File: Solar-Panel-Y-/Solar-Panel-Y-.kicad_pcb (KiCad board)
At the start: 6 copper layers, 64 x 58 mm, 67 parts, among them J1 FFC2B28-10-G, J2 BATTERY CONNECTOR, J3 B2B-PH-SM4-TB_LF__SN_, U1 Value, U2 TSL2561, U3 SW_SPDT, U4 SW_SPDT

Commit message: Exported Gerbers
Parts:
- added H1: MountingHole, MountingHole:MountingHole_2.2mm_M2_DIN965, F.Cu at (84.9, 44.5)
- added H2: MountingHole, MountingHole:MountingHole_2.2mm_M2_DIN965, F.Cu at (85.0, 84.3)
- added H3: MountingHole, MountingHole:MountingHole_2.2mm_M2_DIN965, F.Cu at (124.8, 84.3)
- added H4: MountingHole, MountingHole:MountingHole_2.2mm_M2_DIN965, F.Cu at (124.8, 44.5)
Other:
- outline, holes or cut-outs redrawn

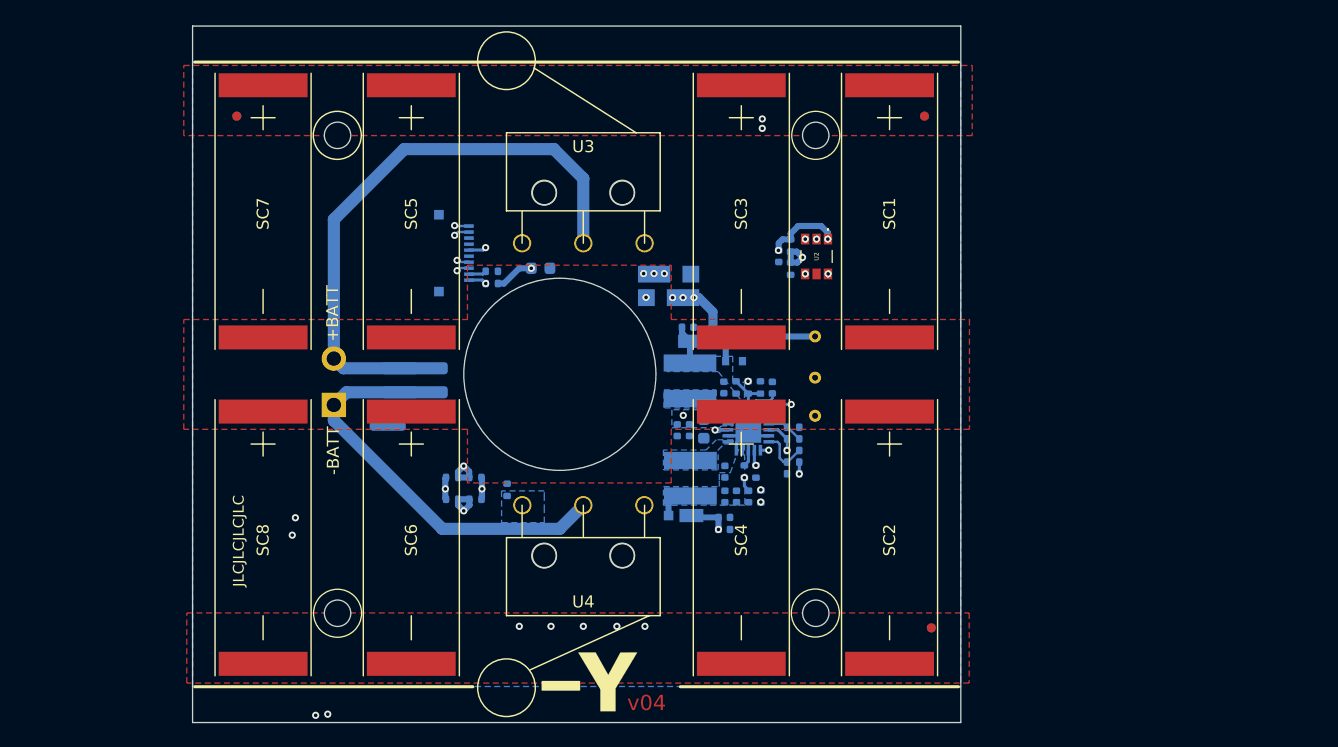
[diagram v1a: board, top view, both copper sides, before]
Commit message: X Board Changes for new Y rails
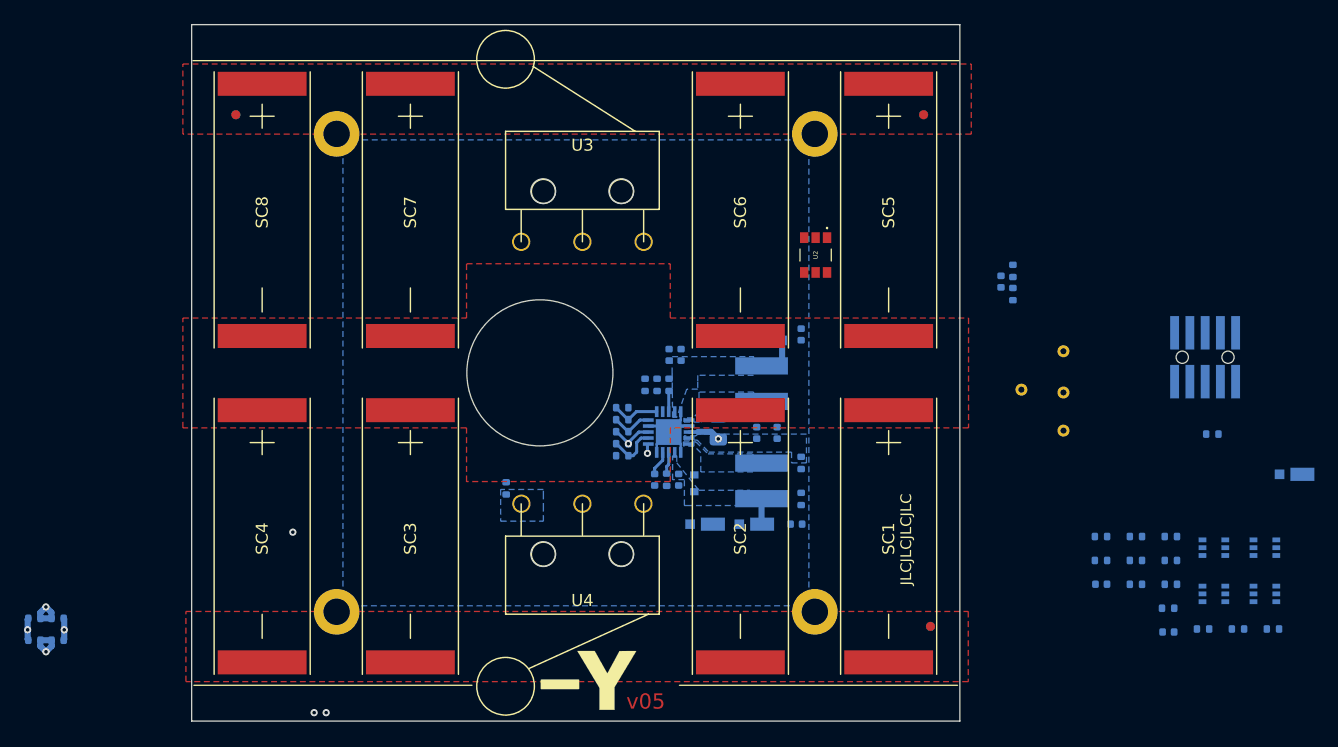
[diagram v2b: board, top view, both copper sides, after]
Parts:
- removed the C1 at (119.2, 74.6)
- removed C14: 100uF, Capacitor_SMD:C_0402_1005Metric
- removed the D5 at (112.5, 58.0)
- removed J2: BATTERY CONNECTOR, solarpanels:SCREWTERMINAL-3.5MM-2_LOCK
- removed J3: B2B-PH-SM4-TB_LF__SN_, Connector_JST:JST_PH_B2B-PH-SM4-TB_1x02-1MP_P2.00mm_Vertical
- removed the R1 at (118.8, 72.5)
- removed the R12 at (120.2, 65.5)
- removed the R13 at (119.2, 65.5)
- removed the R14 at (97.8, 56.9)
- removed the R7 at (119.8, 72.5)
- removed the R8 at (120.2, 74.6)
- added C5: 100uF, Capacitor_SMD:C_0805_2012Metric, B.Cu at (116.7, 68.9)
- added D3: MSS1P4-M3_89A, solarpanels:MICROSMP, B.Cu at (164.7, 72.8)
- added Q1: BSS138DWQ-7, Package_TO_SOT_SMD:SOT-363_SC-70-6, B.Cu at (162.2, 78.9)
- added Q2: MBT2222ADW1T1, Package_TO_SOT_SMD:SOT-363_SC-70-6, B.Cu at (157.9, 82.7)
- added Q3: BSS138DWQ-7, Package_TO_SOT_SMD:SOT-363_SC-70-6, B.Cu at (162.2, 82.7)
- added Q4: MBT2222ADW1T1, Package_TO_SOT_SMD:SOT-363_SC-70-6, B.Cu at (157.9, 78.9)
- added R10: 8.25M, Resistor_SMD:R_0402_1005Metric, B.Cu at (110.6, 65.3)
- added R11: 4.75M, Resistor_SMD:R_0402_1005Metric, B.Cu at (111.6, 65.3)
- added R16: 0, Resistor_SMD:R_0402_1005Metric, B.Cu at (123.6, 71.8)
- added R19: 0, Resistor_SMD:R_0402_1005Metric, B.Cu at (112.6, 65.3)
- added R21: 100K, Resistor_SMD:R_0402_1005Metric, B.Cu at (154.3, 79.9)
- added R22: 0, Resistor_SMD:R_0402_1005Metric, B.Cu at (154.3, 81.9)
- added R23: 0, Resistor_SMD:R_0402_1005Metric, B.Cu at (151.4, 77.9)
- added R24: 10K, Resistor_SMD:R_0402_1005Metric, B.Cu at (162.8, 85.6)
- added R25: 10K, Resistor_SMD:R_0402_1005Metric, B.Cu at (154.1, 83.9)
- added R26: 200K, Resistor_SMD:R_0402_1005Metric, B.Cu at (148.5, 77.9)
- added R27: 680, Resistor_SMD:R_0402_1005Metric, B.Cu at (159.9, 85.6)
- added R28: 100K, Resistor_SMD:R_0402_1005Metric, B.Cu at (151.4, 81.9)
- added R29: 10K, Resistor_SMD:R_0402_1005Metric, B.Cu at (154.3, 77.9)
- added R3: 0, Resistor_SMD:R_0402_1005Metric, B.Cu at (157.8, 69.4)
- added R30: 10K, Resistor_SMD:R_0402_1005Metric, B.Cu at (157.0, 85.6)
- added R31: 200K, Resistor_SMD:R_0402_1005Metric, B.Cu at (148.5, 79.9)
- added R4: 680, Resistor_SMD:R_0402_1005Metric, B.Cu at (151.4, 79.9)
- added TP4: TP, TestPoint:TestPoint_THTPad_D1.0mm_Drill0.5mm, B.Cu at (141.9, 65.7)
- C1: renamed from C5; value 0.1uF -> 1uF
- C10: value 100uF -> 0.1uF; footprint Capacitor_SMD:C_0603_1608Metric -> Capacitor_SMD:C_0402_1005Metric
- C12: value 100uF -> 10nF
- C13: value 0.1uF -> 10nF
- C6: value 100uF -> 1uF; footprint Capacitor_SMD:C_0603_1608Metric -> Capacitor_SMD:C_0402_1005Metric
- C7: value 22uF -> 4.7uF
- C8: value 4.7uF -> 22uF
- D1: value SDM20U40-7 -> SZMM5Z5V1T1G
- D4: value SBDiode -> MSS1P4-M3_89A; footprint solarpanels:SB Diode -> solarpanels:MICROSMP
- H1, H2, H3, H4: footprint MountingHole:MountingHole_2.2mm_M2_DIN965 -> MountingHole:MountingHole_2.2mm_M2_DIN965_Pad
- J1: value FFC2B28-10-G -> FTS-105-01-L-DV-A; footprint solarpanels:GCT_FFC2B28-10-G -> batteryboard:FTS-105-XX-YY-DV-A
- U1: value Value -> BQ25570RGRR
- moved J1 63.2 mm to (157.2, 63.0), turned to 180 degrees
- moved C13 38.0 mm to (154.1, 85.9), turned to 180 degrees
- moved R18 36.7 mm to (61.6, 84.7)
- moved R13 36.7 mm to (61.6, 86.6)
- moved R17 36.7 mm to (59.7, 84.7)
- moved R12 36.7 mm to (59.7, 86.6)
- moved C12 32.2 mm to (148.5, 81.9), turned to 180 degrees
- moved R15 32.0 mm to (123.6, 74.8), turned to 90 degrees
- moved D4 21.0 mm to (115.6, 76.9), turned to 180 degrees
- moved TP1 20.7 mm to (145.4, 69.1)
- moved TP2 20.7 mm to (145.4, 65.9)
- moved TP3 20.7 mm to (145.4, 62.5)
- moved C2 18.7 mm to (123.2, 76.9)
- moved C1 18.6 mm to (140.2, 56.7)
- moved R1 18.6 mm to (141.2, 55.8)
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- renumbered D3 to D5, R17 to R1, R9 to R12, R10 to R13, R11 to R14, R16 to R17, R19 to R18, R18 to R2, R2 to R5, R3 to R6, R4 to R7, R5 to R8, R6 to R9, SC2 to SC1, SC4 to SC2, SC6 to SC3, SC8 to SC4, SC1 to SC5, SC3 to SC6, SC5 to SC7, SC7 to SC8
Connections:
- C11 pad 1: Net-(C11-Pad1) -> +3V3
- C12 pad 1: Net-(C11-Pad1) -> Net-(C12-Pad1)
- C13 pad 1: +3V3 -> Net-(C13-Pad1)
- C6 pad 1: /VBAT -> VOUT_EN
- C7 pad 1: Net-(C11-Pad1) -> Net-(C7-Pad1)
- C9 pad 1: Net-(C10-Pad1) -> Net-(C7-Pad1)
- D2 pad 2: Net-(C11-Pad1) -> Net-(C10-Pad1)
- D4 pad 1: Net-(D4-Pad1) -> /VSOLAR_FULL
- D4 pad 2: GND -> Net-(D3-Pad1)
- J1 pad 1: BATT_P -> BATT_N_SW
- J1 pad 10: COIL_P -> VUSB
- J1 pad 2: BATT_N -> BATT_P_SW
- J1 pad 3: SDA1 -> BATT_P
- J1 pad 4: SCL1 -> +3V3
- J1 pad 5: BURN1 -> GND
- J1 pad 6: +3V3 -> SCL3
- J1 pad 7: GND -> COIL_P
- J1 pad 8: GND -> SDA3
- L2 pad 2: Net-(C11-Pad1) -> Net-(C10-Pad1)
- R14 pad 1: Net-(R11-Pad1) -> Net-(R14-Pad1)
- R15 pad 1: BATT_N -> GND
- R15 pad 2: GND -> Net-(R14-Pad1)
- SC1 pad 1: Net-(D4-Pad1) -> Net-(D3-Pad1)
- SC2 pad 1: Net-(D4-Pad1) -> Net-(D3-Pad1)
- SC3 pad 1: Net-(D4-Pad1) -> Net-(D3-Pad1)
- SC4 pad 1: Net-(D4-Pad1) -> Net-(D3-Pad1)
- SC5 pad 2: Net-(D4-Pad1) -> Net-(D3-Pad1)
- SC6 pad 2: Net-(D4-Pad1) -> Net-(D3-Pad1)
- SC7 pad 2: Net-(D4-Pad1) -> Net-(D3-Pad1)
- SC8 pad 2: Net-(D4-Pad1) -> Net-(D3-Pad1)
- TP1 pad 1: +3V3 -> VSOLAR
- TP3 pad 1: VSOLAR -> +3V3
- U1 pad 14: Net-(C11-Pad1) -> Net-(C10-Pad1)
- U1 pad 19: Net-(C10-Pad1) -> Net-(C7-Pad1)
- U1 pad 3: Net-(R11-Pad1) -> Net-(R14-Pad1)
- U2 pad 4: SCL1 -> SCL3
- U2 pad 6: SDA1 -> SDA3
- U3 pad 2: Net-(J2-Pad2) -> BATT_P_SW
- U4 pad 2: Net-(J2-Pad1) -> BATT_N_SW
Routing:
- net /coil: track 16701.1 -> 14508.4 mm, vias 6 -> 5
- net +3V3: track 68.9 -> 0.00 mm, vias 4 -> 0
- net Net-(J2-Pad2): track 48.3 -> 0.00 mm
- net Net-(J2-Pad1): track 33.8 -> 0.00 mm
- net SDA1: track 33.7 -> 0.00 mm, vias 2 -> 0
- net SCL1: track 31.2 -> 0.00 mm, vias 2 -> 0
- net /VBAT: track 32.2 -> 2.68 mm, vias 2 -> 1
- net COIL_P: track 31.3 -> 3.29 mm, vias 2 -> 1
- net /VSOLAR_FULL: track 25.0 -> 0.00 mm, vias 5 -> 0
- net COIL_N: track 26.6 -> 3.25 mm, vias 2 -> 1
- net VOUT_EN: track 12.2 -> 0.80 mm, vias 2 -> 1
- net VSOLAR: track 12.2 -> 2.04 mm
- net BATT_P: track 6.13 -> 0.00 mm, vias 1 -> 0
- net Net-(C10-Pad1): track 7.45 -> 1.52 mm, vias 2 -> 0
- net Net-(R1-Pad1): track 5.69 -> 0.00 mm, vias 2 -> 0
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- added copper zone on In3.Cu, net GND
- added copper zone on F.Cu, net Net-(D3-Pad1)
- removed copper zone on B.Cu, net Net-(C11-Pad1)
- removed copper zone on F.Cu, net Net-(D4-Pad1)
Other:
- outline, holes or cut-outs redrawn
- board text added: "v05"
- board text removed: "+BATT"
- board text removed: "-BATT"
- board text removed: "1"
- board text removed: "v04"

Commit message: Finished Y- Board
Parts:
- SW1: renamed from U3; footprint solarpanels:D2F-L2-2 -> solarpanels:D2F-L2-A1
- SW2: renamed from U4; footprint solarpanels:D2F-L2 -> solarpanels:D2F-L2-A
- moved D3 76.3 mm to (89.3, 60.5), turned to 0 degrees
- moved R12 59.4 mm to (118.7, 79.2), turned to 0 degrees
- moved R17 59.1 mm to (118.7, 81.1), turned to 0 degrees
- moved R13 55.6 mm to (116.8, 79.2), turned to 0 degrees
- moved R18 55.2 mm to (116.8, 81.1), turned to 0 degrees
- moved R24 47.8 mm to (119.3, 66.1), turned to 90 degrees
- moved Q1 46.1 mm to (118.9, 63.1), turned to -90 degrees
- moved Q3 44.7 mm to (118.9, 71.7), turned to -90 degrees
- moved J1 44.6 mm to (113.0, 68.7)
- moved R3 44.3 mm to (113.8, 74.1)
- moved R27 42.1 mm to (121.2, 69.1)
- moved C10 41.8 mm to (85.9, 79.3)
- moved Q2 41.1 mm to (121.8, 63.1), turned to -90 degrees
- moved C2 38.9 mm to (86.3, 64.3), turned to 180 degrees
- moved R21 38.7 mm to (118.2, 66.1), turned to 90 degrees
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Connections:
- C5 pad 1: /VBAT -> VBAT
- R3 pad 2: /VBAT -> VBAT
- TP4 pad 1: BATT_P -> VBAT
- U1 pad 18: /VBAT -> VBAT
- U2 pad 4: SCL3 -> SCL_LS
- U2 pad 6: SDA3 -> SDA_LS
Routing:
- net /coil: track 14508.4 -> 15508.4 mm
- net VBAT: track 0.00 -> 43.9 mm, vias 0 -> 2
- net BATT_P: track 0.00 -> 31.8 mm, vias 0 -> 1
- net +3V3: track 0.00 -> 25.1 mm, vias 0 -> 7
- net VSOLAR: track 2.04 -> 27.0 mm, vias 0 -> 1
- net /VSOLAR_FULL: track 0.00 -> 23.9 mm, vias 0 -> 4
- net SDA_LS: track 0.00 -> 23.5 mm, vias 0 -> 2
- net SDA3: track 0.00 -> 21.5 mm, vias 0 -> 2
- net BATT_N_SW: track 0.00 -> 18.4 mm
- net BATT_P_SW: track 0.00 -> 17.5 mm
- net SCL3: track 0.00 -> 17.4 mm, vias 0 -> 2
- net COIL_N: track 3.25 -> 17.6 mm, vias 1 -> 2
- net SCL_LS: track 0.00 -> 14.2 mm, vias 0 -> 1
- net Net-(R14-Pad1): track 1.83 -> 15.4 mm, vias 0 -> 2
- net COIL_P: track 3.29 -> 13.6 mm, vias 1 -> 2
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- added copper zone on In1.Cu, net +3V3
- added copper zone on In2.Cu, net +3V3
- added copper zone on In4.Cu, net GND
- added copper zone on B.Cu, net Net-(C7-Pad1)
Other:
- outline, holes or cut-outs redrawn
- board text added: "VBAT"

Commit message: Made Suggested Y- changes
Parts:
- removed SC3, SC7: SolarCell_Small, solarpanels:KXOB25-05X3F
- added J2: BM02B-SRSS-TB, Connector_JST:JST_SH_BM02B-SRSS-TB_1x02-1MP_P1.00mm_Vertical, B.Cu at (75.5, 57.3)
- H1, H2, H3, H4: footprint MountingHole:MountingHole_2.2mm_M2_DIN965_Pad -> MountingHole:MountingHole_3.2mm_M3_DIN965_Pad
- moved SC1 1.05 mm to (131.9, 66.4)
- moved SC5 1.05 mm to (131.9, 41.2)
- moved SC2 1.00 mm to (117.5, 66.4)
- moved SC6 1.00 mm to (117.5, 41.2)
- moved SC4 0.99 mm to (77.7, 66.4)
- moved SC8 0.99 mm to (77.7, 41.2)
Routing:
- net BATT_N_SW: track 18.4 -> 54.2 mm, vias 0 -> 1
- net BATT_P_SW: track 17.5 -> 47.4 mm, vias 0 -> 1
- net /coil: track 15508.4 -> 15486.0 mm
- net GND: vias 3 -> 8
